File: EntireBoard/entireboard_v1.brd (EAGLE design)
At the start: 30 x 30 mm, 44 parts, among them J1 FTSH-105-01-XXX-DV-K, U2 RHD2216_QFN

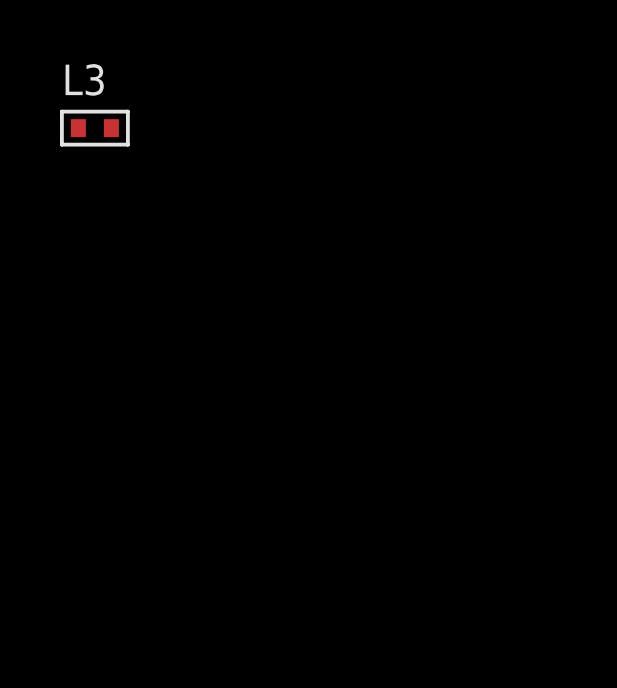
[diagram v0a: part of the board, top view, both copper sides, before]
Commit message: separate branch for test pads
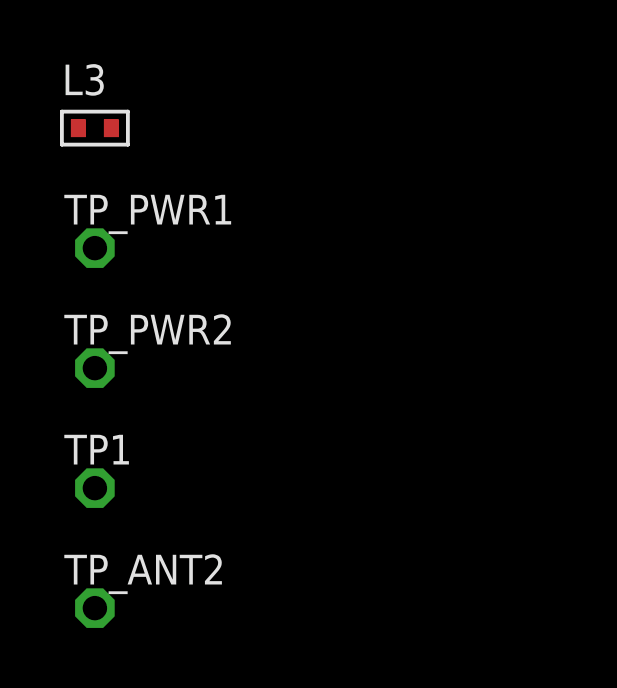
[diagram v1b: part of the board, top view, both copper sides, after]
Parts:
- added TP1, TP_ANT2, TP_PWR1, TP_PWR2: RHD2000_EVAL_BOARD_TESTPOINT_SMALL, AxonMobile:RHD2000_EVAL_BOARD_TESTPOINT_SMALL
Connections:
- net N$11: now also TP1.1
- net N$13: now also TP_PWR2.1
- net N$2: now also TP_ANT2.1
- net VDDS: now also TP_PWR1.1
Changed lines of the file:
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@@
 <attribute name="URL" value="" x="-57" y="-19" size="1.778" layer="27" display="off"/>
+</element>
+<element name="TP_PWR1" library="AxonMobile" package="RHD2000_EVAL_BOARD_TESTPOINT_SMALL" value="RHD2000_EVAL_BOARD_TESTPOINT_SMALL" x="-57" y="-23">
+<attribute name="NAME" x="-58.016" y="-22.2126" size="0.9906" layer="25" font="vector" ratio="12"/>
+</element>
+<element name="TP_PWR2" library="AxonMobile" package="RHD2000_EVAL_BOARD_TESTPOINT_SMALL" value="RHD2000_EVAL_BOARD_TESTPOINT_SMALL" x="-57" y="-27">
+<attribute name="NAME" x="-58.016" y="-26.2126" size="0.9906" layer="25" font="vector" ratio="12"/>
+</element>
+<element name="TP1" library="AxonMobile" package="RHD2000_EVAL_BOARD_TESTPOINT_SMALL" value="RHD2000_EVAL_BOARD_TESTPOINT_SMALL" x="-57" y="-31">
+<attribute name="NAME" x="-58.016" y="-30.2126" size="0.9906" layer="25" font="vector" ratio="12"/>
+</element>
+<element name="TP_ANT2" library="AxonMobile" package="RHD2000_EVAL_BOARD_TESTPOINT_SMALL" value="RHD2000_EVAL_BOARD_TESTPOINT_SMALL" x="-57" y="-35">
+<attribute name="NAME" x="-58.016" y="-34.2126" size="0.9906" layer="25" font="vector" ratio="12"/>
 </element>
 </elements>
@@
 <contactref element="R1" pad="2"/>
 <contactref element="R_CS" pad="P$1"/>
-<wire x1="10.47" y1="19.75" x2="14.62" y2="18.1" width="0" layer="19" extent="1-1"/>
+<contactref element="TP_PWR1" pad="1"/>
+<wire x1="-57.8" y1="22.86" x2="-57" y2="-23" width="0" layer="19" extent="1-1"/>
+<wire x1="-51.45" y1="22.86" x2="-57.8" y2="22.86" width="0" layer="19" extent="1-1"/>
+<wire x1="-45.1" y1="22.86" x2="-51.45" y2="22.86" width="0" layer="19" extent="1-1"/>
+<wire x1="-38.75" y1="22.86" x2="-45.1" y2="22.86" width="0" layer="19" extent="1-1"/>
+<wire x1="-43.83" y1="29.21" x2="-45.1" y2="22.86" width="0" layer="19" extent="1-1"/>
+<wire x1="-46.4566" y1="40.64" x2="-43.83" y2="29.21" width="0" layer="19" extent="1-1"/>
+<wire x1="-38.65" y1="44.45" x2="-46.4566" y2="40.64" width="0" layer="19" extent="1-1"/>
+<wire x1="-44.945" y1="49.53" x2="-38.65" y2="44.45" width="0" layer="19" extent="1-1"/>
+<wire x1="-21.09" y1="40.64" x2="-38.65" y2="44.45" width="0" layer="19" extent="1-1"/>
+<wire x1="10.47" y1="19.75" x2="-21.09" y2="40.64" width="0" layer="19" extent="1-1"/>
+<wire x1="14.62" y1="18.1" x2="10.47" y2="19.75" width="0" layer="19" extent="1-1"/>
 <wire x1="12.97" y1="12.95" x2="14.62" y2="18.1" width="0" layer="19" extent="1-1"/>
 <wire x1="8.47" y1="12.95" x2="12.97" y2="12.95" width="0" layer="19" extent="1-1"/>
-<wire x1="-21.09" y1="40.64" x2="10.47" y2="19.75" width="0" layer="19" extent="1-1"/>
-<wire x1="-38.65" y1="44.45" x2="-21.09" y2="40.64" width="0" layer="19" extent="1-1"/>
-<wire x1="-44.945" y1="49.53" x2="-38.65" y2="44.45" width="0" layer="19" extent="1-1"/>
-<wire x1="-46.4566" y1="40.64" x2="-38.65" y2="44.45" width="0" layer="19" extent="1-1"/>
-<wire x1="-43.83" y1="29.21" x2="-46.4566" y2="40.64" width="0" layer="19" extent="1-1"/>
-<wire x1="-45.1" y1="22.86" x2="-43.83" y2="29.21" width="0" layer="19" extent="1-1"/>
-<wire x1="-51.45" y1="22.86" x2="-45.1" y2="22.86" width="0" layer="19" extent="1-1"/>
-<wire x1="-57.8" y1="22.86" x2="-51.45" y2="22.86" width="0" layer="19" extent="1-1"/>
-<wire x1="-38.75" y1="22.86" x2="-45.1" y2="22.86" width="0" layer="19" extent="1-1"/>
 </signal>
 <signal name="VCC">
@@
 <contactref element="R_CS" pad="P$2"/>
 <contactref element="POWER_IND" pad="1"/>
-<wire x1="-47.5234" y1="40.64" x2="-37.55" y2="44.45" width="0" layer="19" extent="1-1"/>
+<contactref element="TP_PWR2" pad="1"/>
+<wire x1="-47.5234" y1="40.64" x2="-57" y2="-27" width="0" layer="19" extent="1-1"/>
+<wire x1="-37.55" y1="44.45" x2="-47.5234" y2="40.64" width="0" layer="19" extent="1-1"/>
 </signal>
 <signal name="N$6">
@@
 <contactref element="U$2" pad="FEED"/>
 <contactref element="CURRENT-SENSE" pad="P$2"/>
-<wire x1="-32.47" y1="44.45" x2="13.04" y2="22.44" width="0" layer="19" extent="1-1"/>
+<contactref element="TP_ANT2" pad="1"/>
+<wire x1="-32.47" y1="44.45" x2="-57" y2="-35" width="0" layer="19" extent="1-1"/>
+<wire x1="13.04" y1="22.44" x2="-32.47" y2="44.45" width="0" layer="19" extent="1-1"/>
 </signal>
 <signal name="N$11">
 <contactref element="C11" pad="2"/>
 <contactref element="CURRENT-SENSE" pad="P$1"/>
-<wire x1="-29.83" y1="29.21" x2="-33.57" y2="44.45" width="0" layer="19" extent="1-1"/>
+<contactref element="TP1" pad="1"/>
+<wire x1="-29.83" y1="29.21" x2="-57" y2="-31" width="0" layer="19" extent="1-1"/>
+<wire x1="-33.57" y1="44.45" x2="-29.83" y2="29.21" width="0" layer="19" extent="1-1"/>
 </signal>
 <signal name="N$7">
